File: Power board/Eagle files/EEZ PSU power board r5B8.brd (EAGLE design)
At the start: 74 x 150 mm, 270 parts, among them IC1 LTC3864, IC10 REF5025, IC11 DAC8552, IC12 ADG465SOT-23, IC13 TS5A9411DCKT, IC14 ADS1120, IC15 LP339D, IC2 MC79L05, IC3 MC78L05, IC4 LM5574, IC5 LP2951SO8, IC6 TL072D, IC7 TL072D, IC8 OP27GSZ, IC9 MCP23S08-E/SO, Q1 SUD19P06-60, Q10 MMBT5401, Q11 MMBT5401, Q12 MMBT5551, Q13 MMBT5551, Q14 BSS84P, Q15 2N7002, Q16 MMBT5551, Q17 MMBT5401, Q18 MMBT5551, Q19 MMBT5551, Q2 MMBT5401, Q3 2N7002, Q4 IRFP250N, Q5 BC857C, Q6 BC846C, Q7 BCP56-16.115, Q8 IRFR5410, Q9 BCP56-16.115, X1 282836-3, X2 282836-2, X3 SSW-113-02-T-D-RA

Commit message: Power board R28, R29
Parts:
- R28: value 0R1/3W -> R080/3W; device EEZ_Lib1:R_2512+0411/15 -> rcl:R2512
- R29: device EEZ_Lib1:R_2512+0411/15 -> rcl:R2512
- TR1: value MSD1260-824 -> SRF0703-821M
- moved Q6 0.57 mm to (71.4, 38.8)
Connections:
- net N$146: no longer R29.1.1
- net OUT+: no longer R28.2.1, R29.2.1
- net Q4_OUT: no longer R28.1.1
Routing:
- net OUT+: track 182.8 -> 186.5 mm, vias 12 -> 19
- net Q4_OUT: track 39.5 -> 41.6 mm, vias 6 -> 10
- net N$146: track 20.3 -> 20.6 mm, vias 1 -> 2
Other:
- board text added: "* Check instructions for R13 installation"
- board text removed: "* Check instructions for R16 and R79 installation"

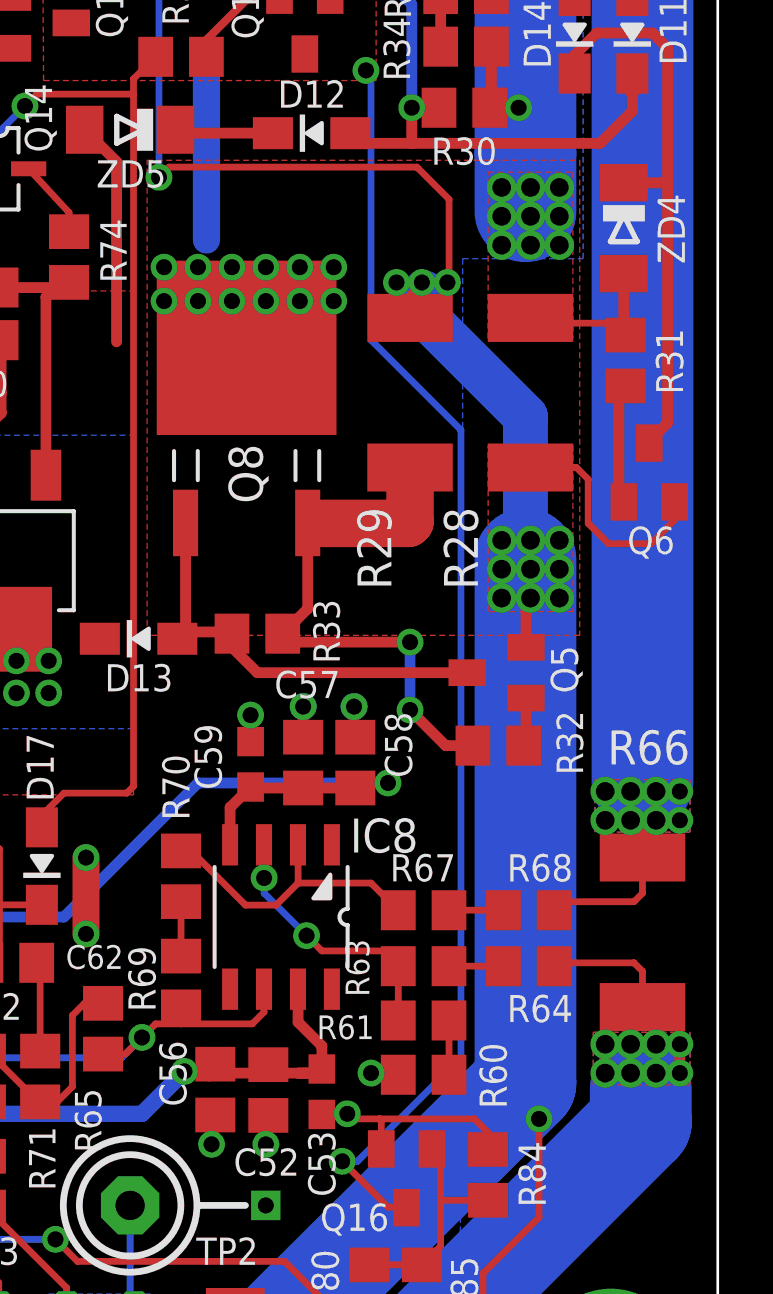
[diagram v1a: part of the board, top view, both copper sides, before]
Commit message: Power board R28, R29 PCB layout, BOM corrections
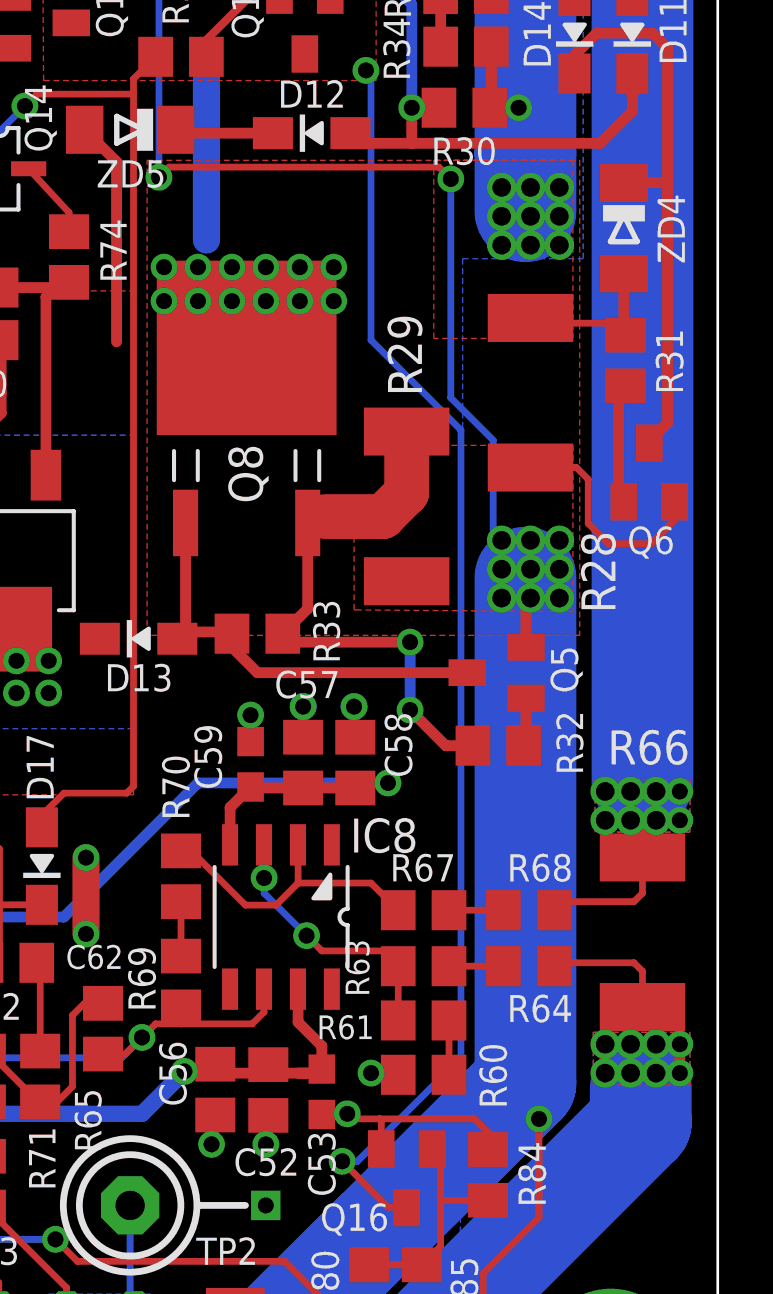
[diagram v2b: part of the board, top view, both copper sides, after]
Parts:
- moved R29 4.26 mm to (62.4, 37.5), turned to 270 degrees
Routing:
- net OUT+: track 186.5 -> 179.9 mm, vias 19 -> 17
- net N$146: track 20.6 -> 21.4 mm

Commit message: Rt value corrections for AUX PS and Power board
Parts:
- R22: value 18K -> 20K
